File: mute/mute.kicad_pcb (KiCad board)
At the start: 2 copper layers, 54.6 x 38.1 mm, 24 parts, among them J1 Conn_01x03, J2 tw in, J3 tw out, J4 w in, J5 w out, K1 G6S-2, Q1 npn, Q2 npn, Q3 pnp

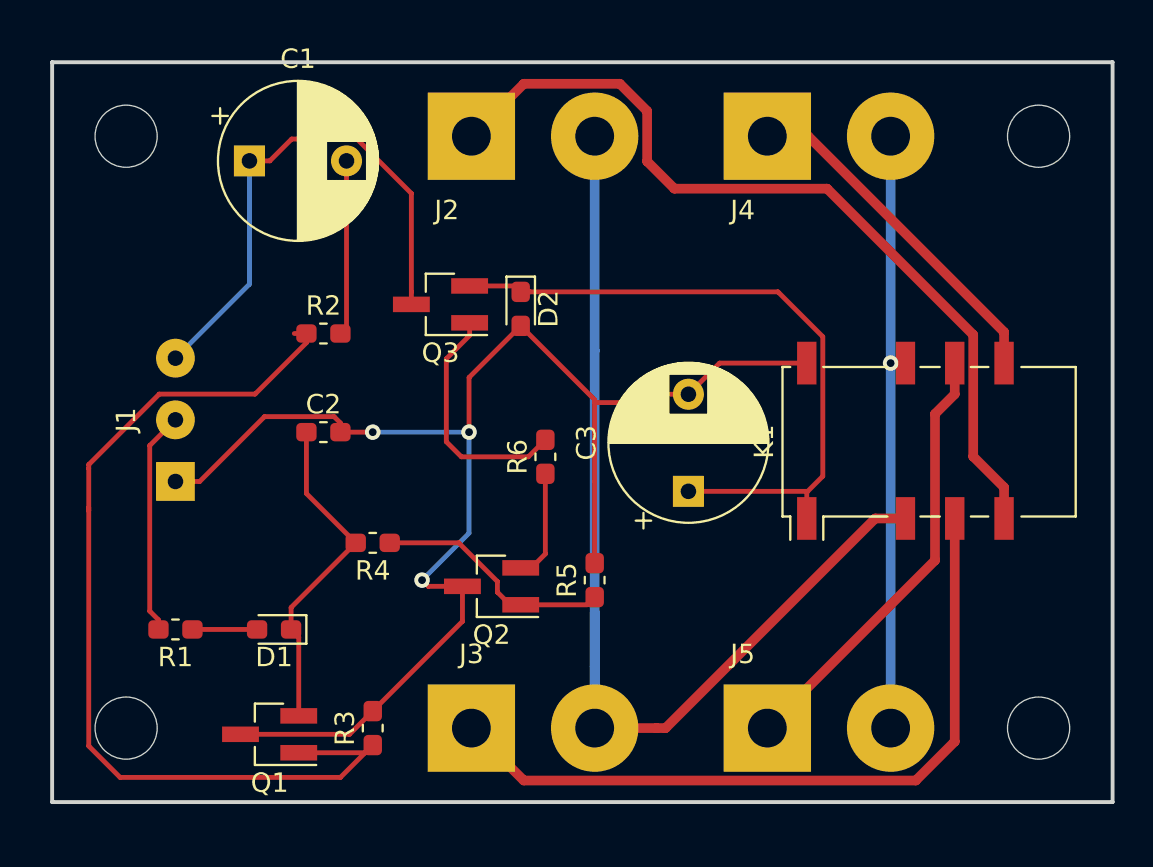
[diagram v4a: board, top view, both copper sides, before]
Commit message: Better footprints after another simulation run.
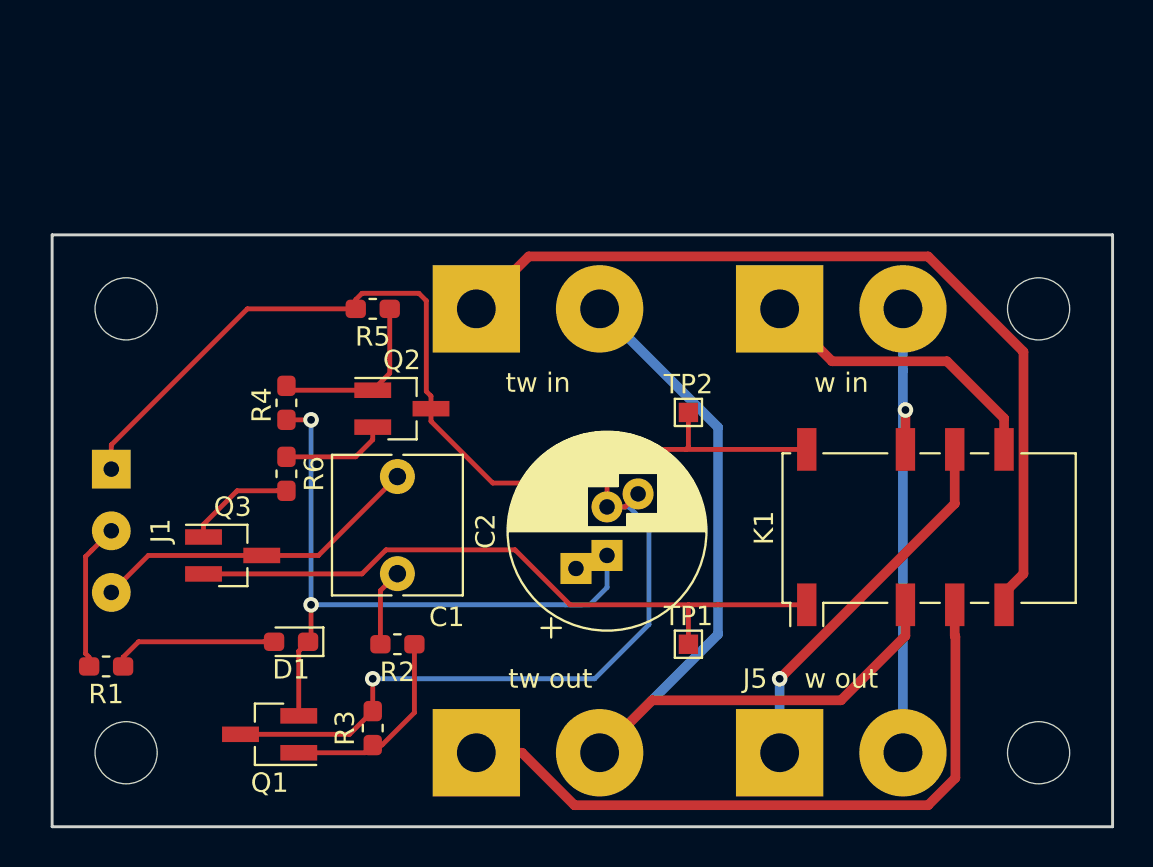
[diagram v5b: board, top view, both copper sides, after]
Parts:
- removed C3: 1u, Capacitor_THT:CP_Radial_D8.0mm_P5.00mm
- removed D2: D, Diode_SMD:D_0603_1608Metric_Pad1.05x0.95mm_HandSolder
- added TP1: TestPoint, TestPoint:TestPoint_Pad_1.0x1.0mm, F.Cu at (82.3, 110.0)
- added TP2: TestPoint, TestPoint:TestPoint_Pad_1.0x1.0mm, F.Cu at (82.3, 98.0)
- C1: value 1u -> 100n; footprint Capacitor_THT:CP_Radial_D8.0mm_P5.00mm -> Capacitor_THT:C_Rect_L7.0mm_W6.5mm_P5.00mm
- C2: value 1u -> 3.3u; footprint Capacitor_SMD:C_0603_1608Metric_Pad1.05x0.95mm_HandSolder -> Capacitor_THT:CP_Radial_D10.0mm_P2.50mm_P5.00mm
- moved R5 18.1 mm to (66.0, 92.7), turned to 180 degrees
- moved C1 18.0 mm to (67.3, 101.3), turned to 270 degrees
- moved Q3 16.8 mm to (58.8, 105.4), turned to 0 degrees
- moved R2 16.4 mm to (67.3, 110.0), turned to 180 degrees
- moved C2 15.9 mm to (78.1, 105.4), turned to 90 degrees
- moved R6 13.4 mm to (61.6, 101.2), turned to 270 degrees
- moved Q2 10.2 mm to (67.5, 97.9), turned to 0 degrees
- moved J4 8.91 mm to (87.0, 92.7)
- moved J2 8.89 mm to (71.4, 92.7)
- moved H1 8.89 mm to (53.3, 92.7)
- moved H3 8.89 mm to (100.3, 92.7)
- moved R4 8.47 mm to (61.6, 97.5), turned to 270 degrees
- moved K1 4.45 mm to (94.7, 104.0)
- moved R1 4.05 mm to (52.3, 111.1)
- moved J1 3.36 mm to (52.6, 101.0), turned to 270 degrees
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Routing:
- net Net-(Q1-Pad1): track 49.5 -> 10.3 mm
- net Net-(C2-Pad1): track 17.2 -> 36.8 mm, vias 0 -> 2
- net Net-(C1-Pad1): track 27.4 -> 17.2 mm
- net GND: track 75.8 -> 85.9 mm, vias 3 -> 1
- net Net-(J2-Pad2): track 56.9 -> 47.8 mm
- net Net-(Q3-Pad1): track 12.4 -> 5.64 mm
- net Net-(J4-Pad2): track 31.2 -> 24.9 mm
- net Net-(D1-Pad2): track 3.33 -> 8.58 mm
- net Net-(C1-Pad2): track 9.02 -> 4.00 mm
- net /ACSense: track 11.5 -> 7.61 mm
- net Net-(J5-Pad1): track 22.8 -> 19.4 mm, vias 0 -> 1
- net Net-(Q2-Pad1): track 12.4 -> 9.09 mm
- net Net-(J3-Pad1): track 38.3 -> 35.3 mm
- net Net-(J4-Pad1): track 18.0 -> 15.5 mm
- net Net-(J2-Pad1): track 44.0 -> 44.8 mm
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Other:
- board size 54.6 x 38.1 mm -> 54.6 x 30.5 mm
